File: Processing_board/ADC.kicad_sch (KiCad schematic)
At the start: 59 parts, among them U10 ADS1299IPAG, U11 ADS1299IPAG

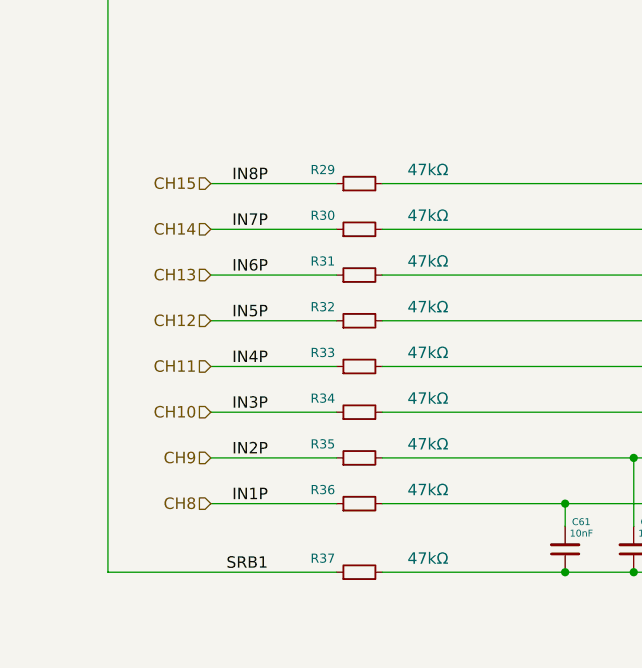
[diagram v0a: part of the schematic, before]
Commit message: fix,feat: all wires to ADC in place but for GND/VDD (A+D)
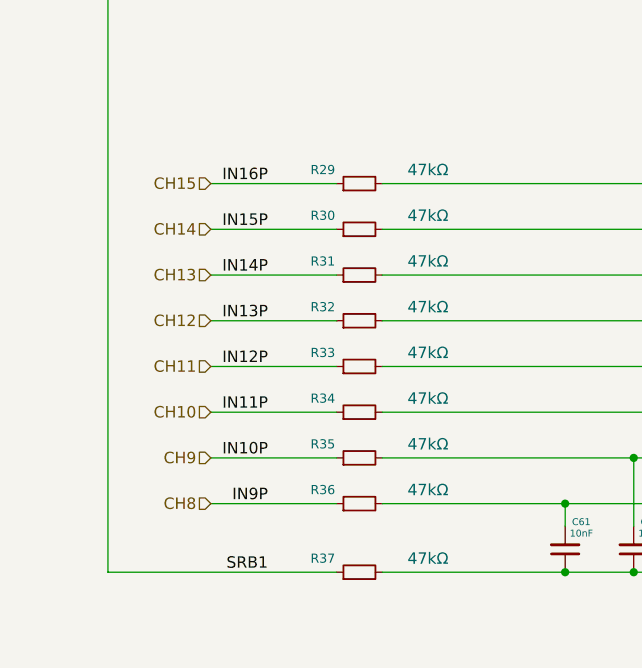
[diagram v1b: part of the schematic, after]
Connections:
- net CH0: no longer R36.1
- net CH1: no longer R35.1
- net CH10: no longer R25.1
- net CH11: no longer R24.1
- net CH12: no longer R23.1
- net CH13: no longer R22.1
- net CH14: no longer R12.1
- net CH15: no longer R11.1
- new net CH2: R25.1
- new net CH3: R24.1
- new net CH4: R23.1
- new net CH5: R22.1
- new net CH6: R12.1
- new net CH7: R11.1
- new net CH8: R36.1
- new net CH9: R35.1
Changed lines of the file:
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@@
 		)
 	)
-	(label "IN8P"
+	(label "IN16P"
 		(at 40.64 154.94 180)
 		(effects
@@
 		)
 	)
-	(label "IN4P"
+	(label "IN12P"
 		(at 40.64 175.26 180)
 		(effects
@@
 		)
 	)
-	(label "IN2P"
+	(label "IN10P"
 		(at 40.64 185.42 180)
 		(effects
@@
 		)
 	)
-	(label "IN7P"
+	(label "IN15P"
 		(at 40.64 160.02 180)
 		(effects
@@
 		)
 	)
-	(label "IN3P"
+	(label "IN11P"
 		(at 40.64 180.34 180)
 		(effects
@@
 		)
 	)
-	(label "IN6P"
+	(label "IN14P"
 		(at 40.64 165.1 180)
 		(effects
@@
 		)
 	)
-	(label "IN5P"
+	(label "IN13P"
 		(at 40.64 170.18 180)
 		(effects
@@
 		)
 	)
-	(label "IN1P"
+	(label "IN9P"
 		(at 40.64 190.5 180)
 		(effects

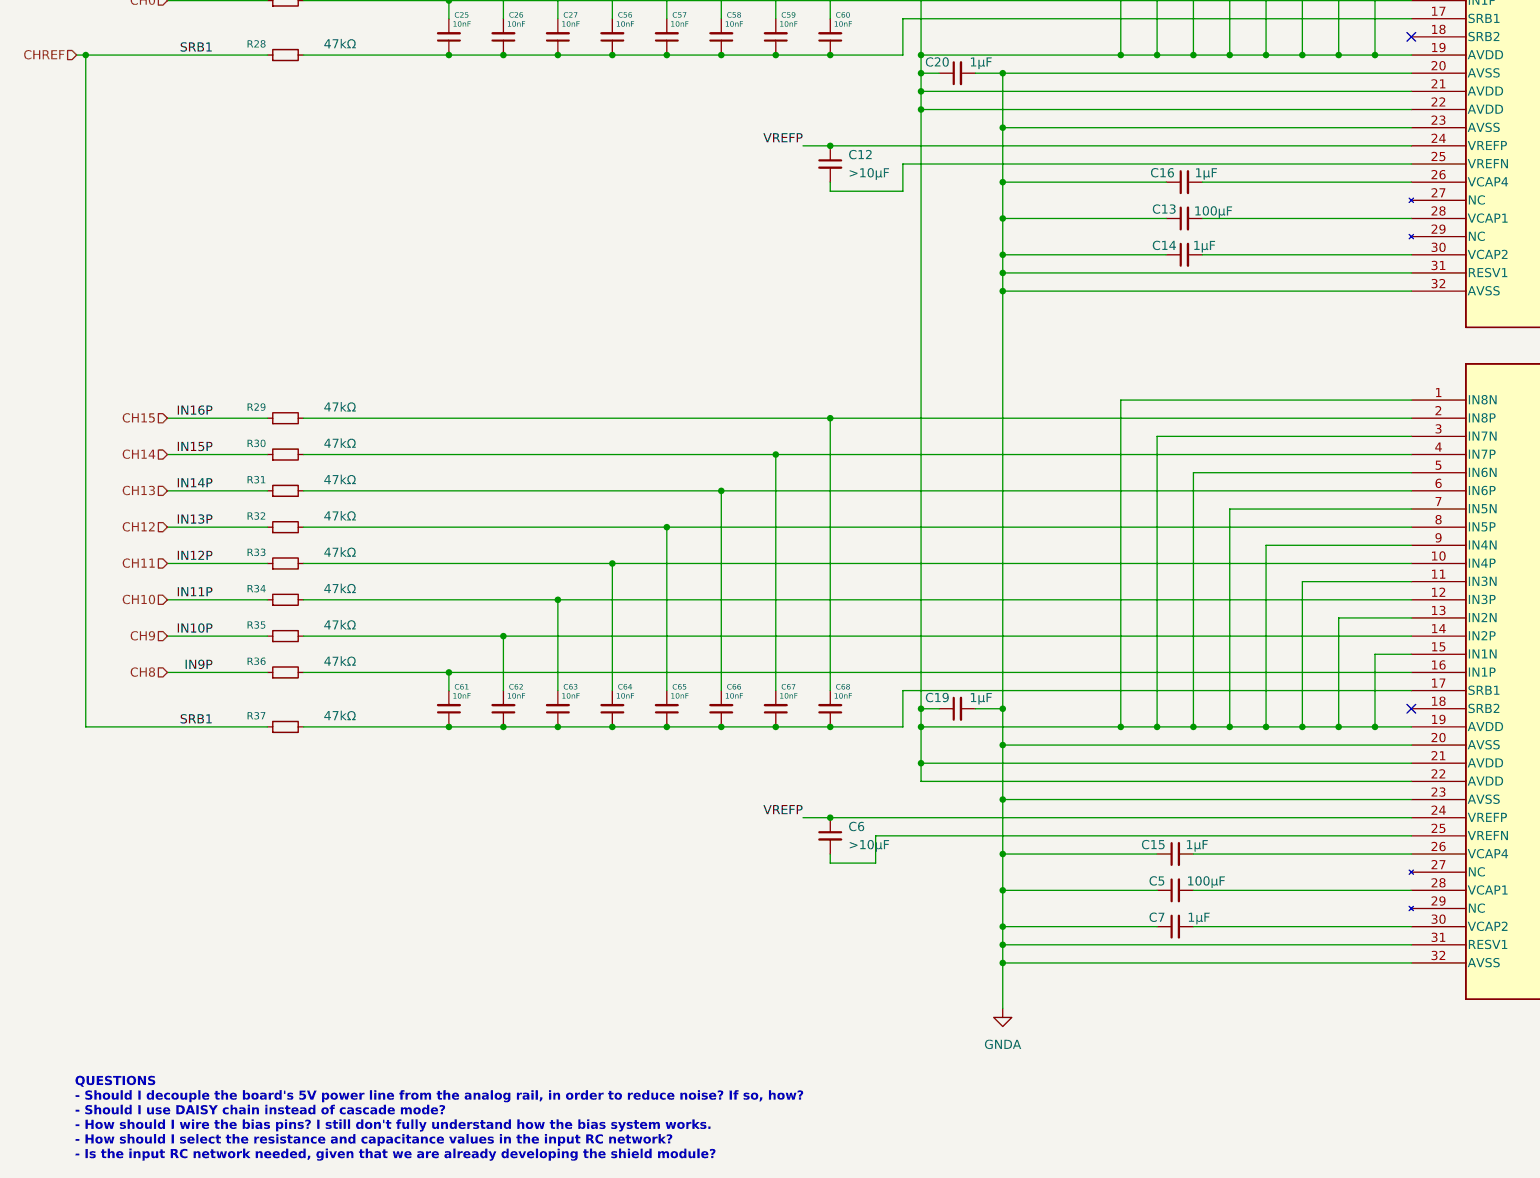
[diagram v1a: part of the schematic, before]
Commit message: fix: mistake in power supply schematics
Previous schematics did not match the datasheet spec for unipolar power supply
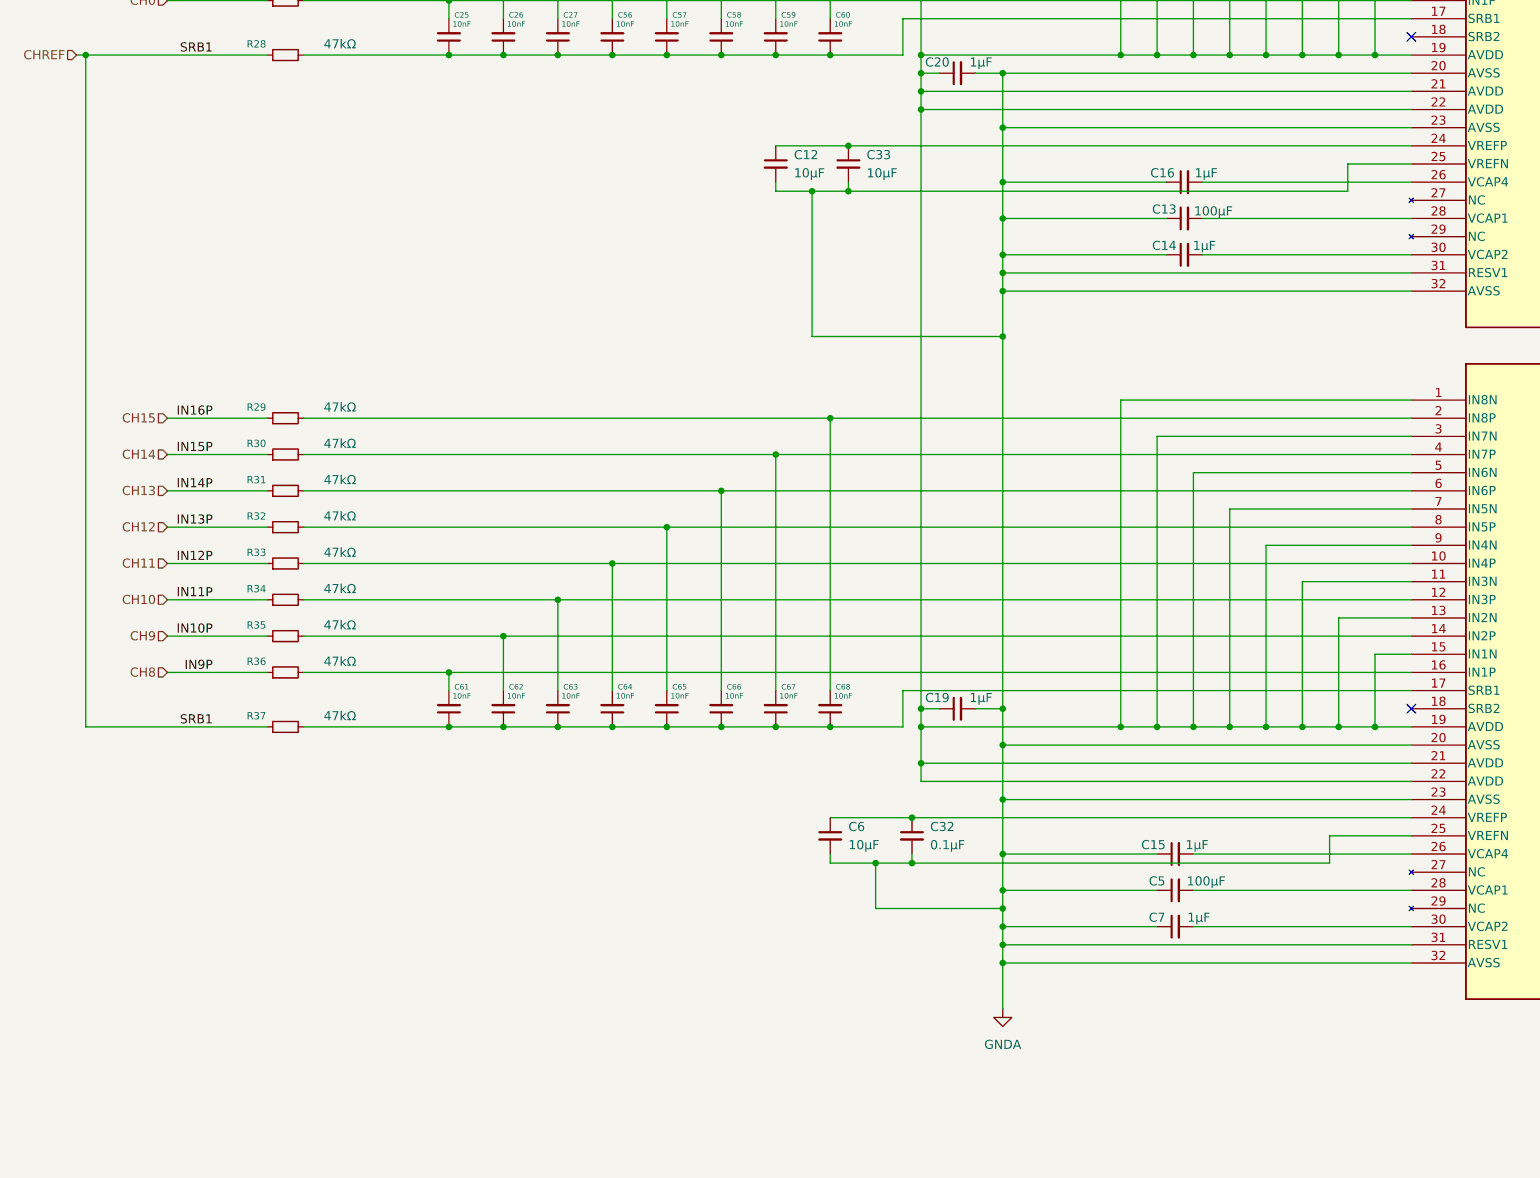
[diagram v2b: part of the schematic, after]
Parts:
- added C32: 0.1µF, symbol Device:C_Small
- added C33: 10μF, Capacitor_SMD:C_0805_2012Metric, symbol Device:C_Small
- C12, C6: value >10μF -> 10μF
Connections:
- net GNDA: now also C12.2, C6.2, U10.25 (VREFN), U11.25 (VREFN), C32.2, C33.2
- net VREFP: no longer names the net of C6.1, U11.24 (VREFP)
- net VREFP: now also C32.1; no longer C12.1, U10.24 (VREFP)
- new net: C12.1, C33.1, U10.24 (VREFP)
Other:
- note removed: "QUESTIONS - Should I decouple the board's 5V power line from the analog rail, in order to reduce noise? If so, how? - Should I use DAISY chain instead of cascade mode? - How should I wire the bias pins? I still don't fully understand how the bias system works. - How should I select the resistance and capacitance values in the input RC network? - Is the input RC network needed, given that we are a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"
- moved on the sheet: C12

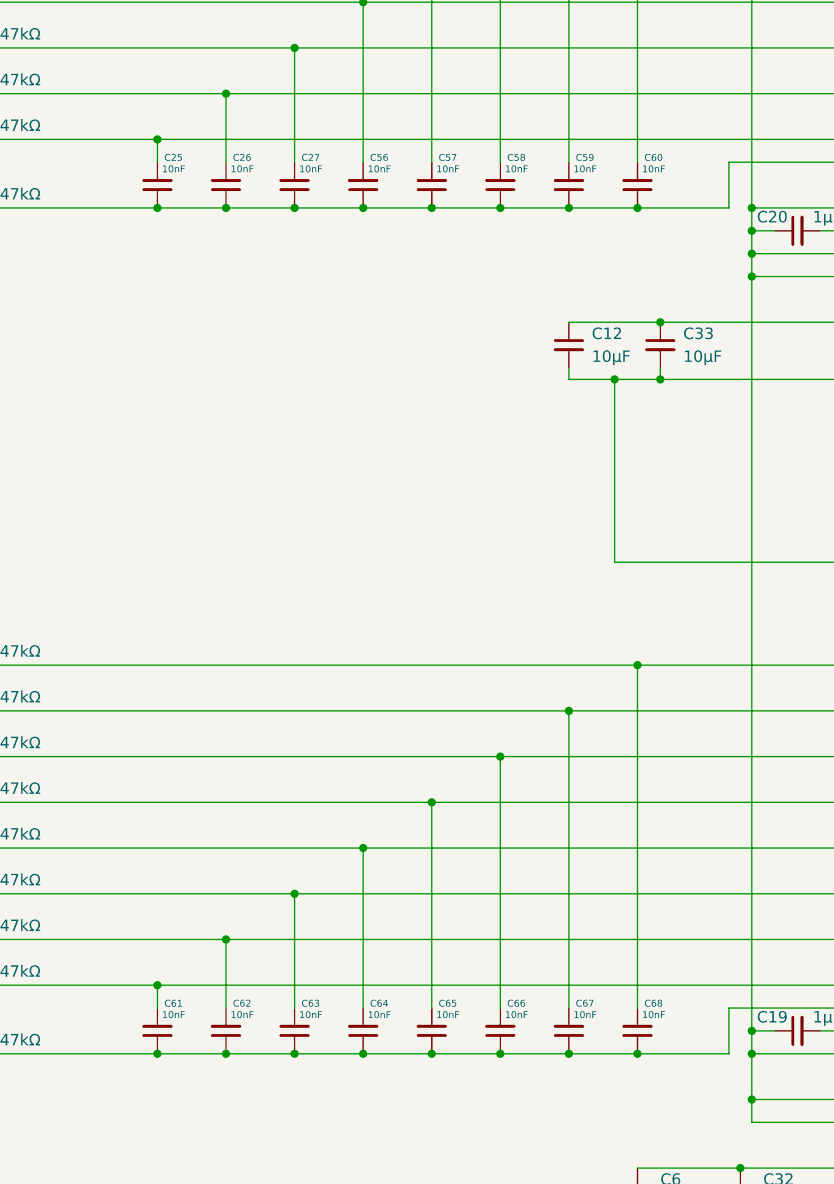
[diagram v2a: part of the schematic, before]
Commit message: fix: changed antialiasing caps values (10nF --> 20nF)
Previous values gave a cutoff frequency of ~350Hz which would cause problems with reconstruction
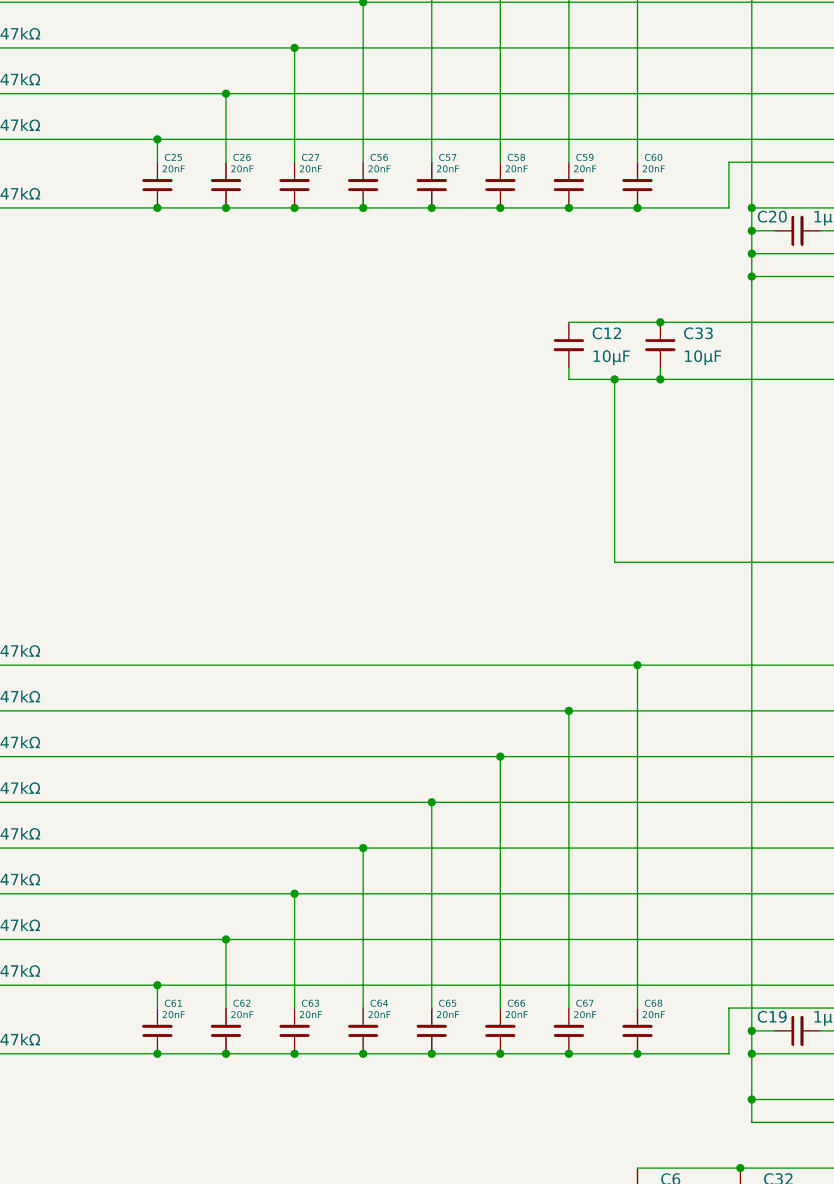
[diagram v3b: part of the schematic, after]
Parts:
- C25, C26, C27, C56, C57, C58, C59, C60, C61, C62, C63, C64, C65, C66, C67, C68: value 10nF -> 20nF
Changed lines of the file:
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@@
 			)
 		)
-		(property "Value" "10nF"
+		(property "Value" "20nF"
 			(at 89.408 99.822 0)
 			(effects
@@
 			)
 		)
-		(property "Value" "10nF"
+		(property "Value" "20nF"
 			(at 127.508 193.802 0)
 			(effects
@@
 			)
 		)
-		(property "Value" "10nF"
+		(property "Value" "20nF"
 			(at 74.168 193.802 0)
 			(effects
@@
 			)
 		)
-		(property "Value" "10nF"
+		(property "Value" "20nF"
 			(at 119.888 193.802 0)
 			(effects
@@
 			)
 		)
-		(property "Value" "10nF"
+		(property "Value" "20nF"
 			(at 104.648 193.802 0)
 			(effects
@@
 			)
 		)
-		(property "Value" "10nF"
+		(property "Value" "20nF"
 			(at 119.888 99.822 0)
 			(effects
@@
 			)
 		)
-		(property "Value" "10nF"
+		(property "Value" "20nF"
 			(at 104.648 99.822 0)
 			(effects
@@
 			)
 		)
-		(property "Value" "10nF"
+		(property "Value" "20nF"
 			(at 74.168 99.822 0)
 			(effects
@@
 			)
 		)
-		(property "Value" "10nF"
+		(property "Value" "20nF"
 			(at 81.788 99.822 0)
 			(effects
@@
 			)
 		)
-		(property "Value" "10nF"
+		(property "Value" "20nF"
 			(at 97.028 193.802 0)
 			(effects
@@
 			)
 		)
-		(property "Value" "10nF"
+		(property "Value" "20nF"
 			(at 89.408 193.802 0)
 			(effects
@@
 			)
 		)
-		(property "Value" "10nF"
+		(property "Value" "20nF"
 			(at 112.268 99.822 0)
 			(effects
@@
 			)
 		)
-		(property "Value" "10nF"
+		(property "Value" "20nF"
 			(at 81.788 193.802 0)
 			(effects
@@
 			)
 		)
-		(property "Value" "10nF"
+		(property "Value" "20nF"
 			(at 112.268 193.802 0)
 			(effects
@@
 			)
 		)
-		(property "Value" "10nF"
+		(property "Value" "20nF"
 			(at 127.508 99.822 0)
 			(effects
@@
 			)
 		)
-		(property "Value" "10nF"
+		(property "Value" "20nF"
 			(at 97.028 99.822 0)
 			(effects
